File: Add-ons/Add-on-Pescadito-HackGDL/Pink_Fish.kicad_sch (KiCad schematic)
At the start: 16 parts, among them J2 Conn_02x03_Odd_Even, SW3 SW_RST, SW4 On, U2 PY32F002AA15M6TU

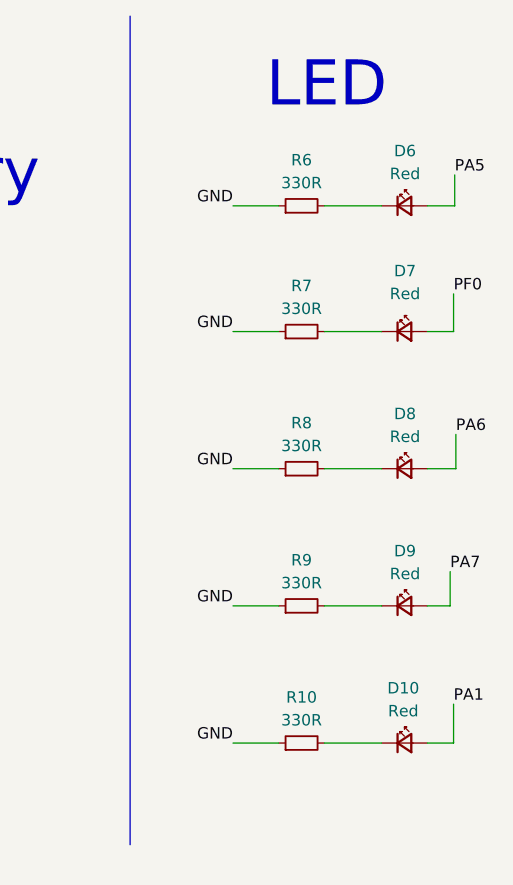
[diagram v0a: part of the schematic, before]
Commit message: feat(Hw):Update_Labels
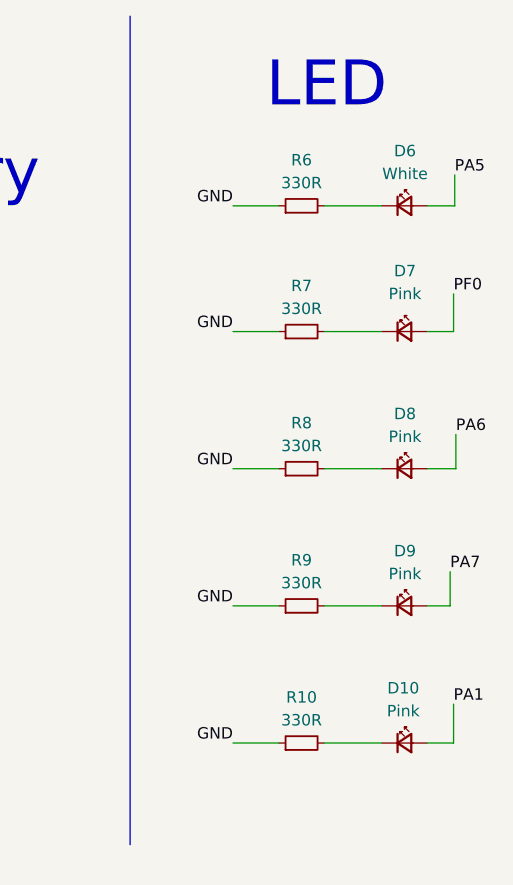
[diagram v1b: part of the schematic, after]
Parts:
- D10, D7, D8, D9: value Red -> Pink; LCSC# C965812 -> C965821
- D6: value Red -> White; LCSC# C965812 -> C84258
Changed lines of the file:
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@@
 			)
 		)
-		(property "Value" "Red"
+		(property "Value" "Pink"
 			(at 183.8325 43.307 0)
 			(effects
@@
 			)
 		)
-		(property "LCSC#" "C965812"
+		(property "LCSC#" "C965821"
 			(at 183.769 47.498 0)
 			(effects
@@
 			)
 		)
-		(property "Value" "Red"
+		(property "Value" "Pink"
 			(at 183.642 89.662 0)
 			(effects
@@
 			)
 		)
-		(property "LCSC#" "C965812"
+		(property "LCSC#" "C965821"
 			(at 183.769 93.218 0)
 			(effects
@@
 			)
 		)
-		(property "Value" "Red"
+		(property "Value" "White"
 			(at 183.8325 29.972 0)
 			(effects
@@
 			)
 		)
-		(property "LCSC#" "C965812"
+		(property "LCSC#" "C84258"
 			(at 183.769 33.528 0)
 			(effects
@@
 			)
 		)
-		(property "Value" "Red"
+		(property "Value" "Pink"
 			(at 183.8325 59.182 0)
 			(effects
@@
 			)
 		)
-		(property "LCSC#" "C965812"
+		(property "LCSC#" "C965821"
 			(at 183.769 62.738 0)
 			(effects
@@
 			)
 		)
-		(property "Value" "Red"
+		(property "Value" "Pink"
 			(at 183.8325 74.422 0)
 			(effects
@@
 			)
 		)
-		(property "LCSC#" "C965812"
+		(property "LCSC#" "C965821"
 			(at 183.769 77.978 0)
 			(effects
